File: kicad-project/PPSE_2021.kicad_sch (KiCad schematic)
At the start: 0 parts

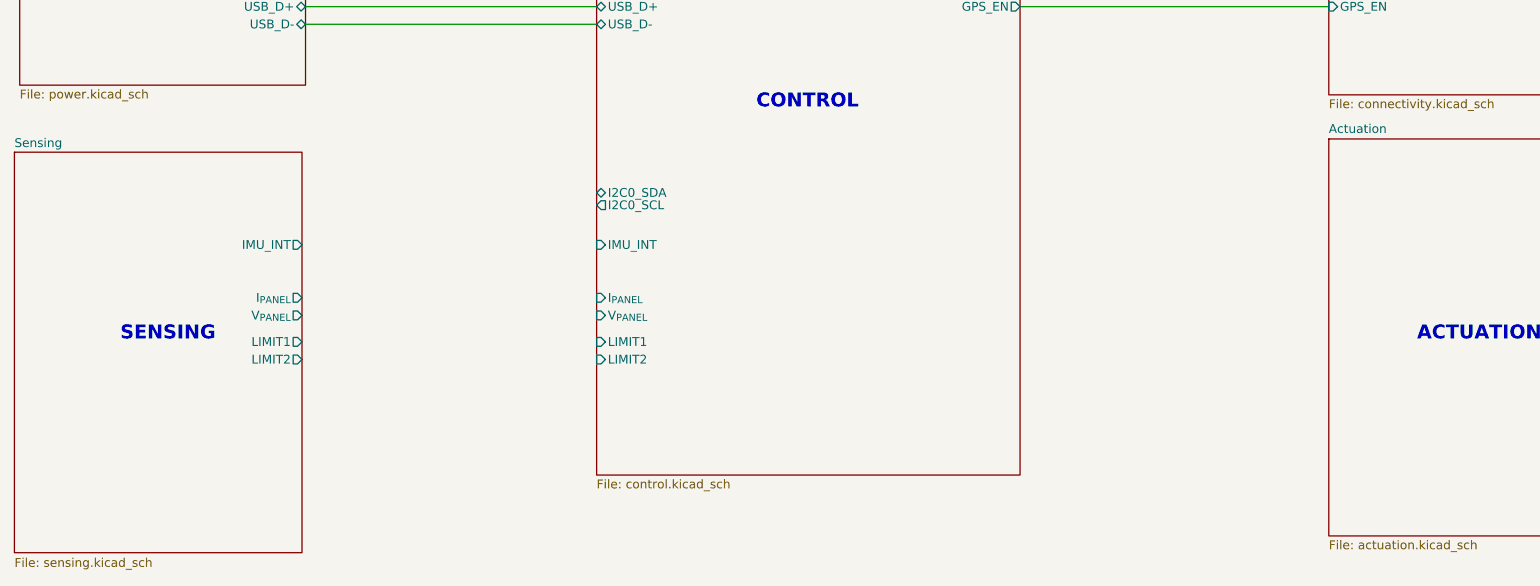
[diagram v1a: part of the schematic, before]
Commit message: hw: update root pin and usb connector
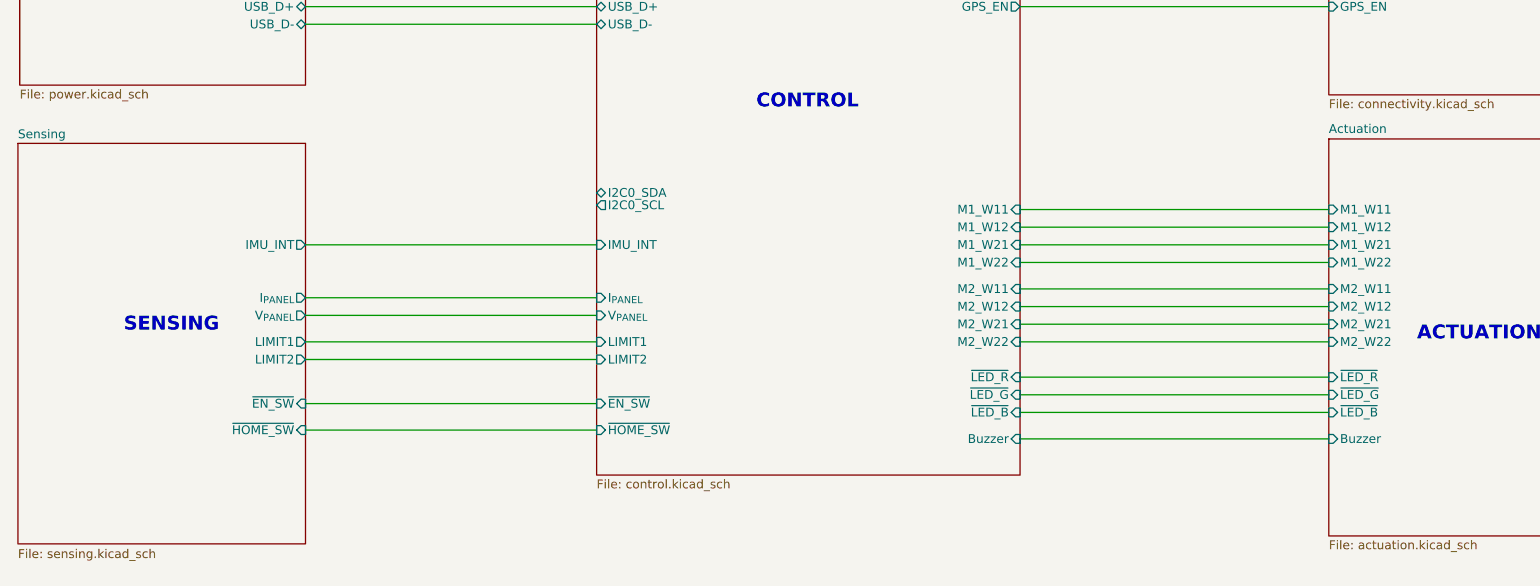
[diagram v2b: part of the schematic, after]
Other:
- sheet Actuation ports: added Buzzer, M1_W11, M1_W12, M1_W21, M1_W22, M2_W11, M2_W12, M2_W21, M2_W22, ~{LED_B}, ~{LED_G}, ~{LED_R}; removed none
- sheet Control ports: added Buzzer, M1_W11, M1_W12, M1_W21, M1_W22, M2_W11, M2_W12, M2_W21, M2_W22, ~{EN_SW}, ~{HOME_SW}, ~{LED_B}, ~{LED_G}, ~{LED_R}; removed none
- sheet Sensing ports: added ~{EN_SW}, ~{HOME_SW}; removed none
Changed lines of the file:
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@@
     (title "Main")
   )
+  (wire (pts (xy 71.12 111.76) (xy 113.03 111.76))
+    (stroke (width 0) (type default) (color 0 0 0 0))
+  )
+  (wire (pts (xy 173.99 116.84) (xy 218.44 116.84))
+    (stroke (width 0) (type default) (color 0 0 0 0))
+  )
+  (wire (pts (xy 173.99 92.71) (xy 218.44 92.71))
+    (stroke (width 0) (type default) (color 0 0 0 0))
+  )
+  (wire (pts (xy 71.12 120.65) (xy 113.03 120.65))
+    (stroke (width 0) (type default) (color 0 0 0 0))
+  )
   (wire (pts (xy 71.12 63.5) (xy 113.03 63.5))
     (stroke (width 0) (type default) (color 0 0 0 0))
   )
+  (wire (pts (xy 173.99 125.73) (xy 218.44 125.73))
+    (stroke (width 0) (type default) (color 0 0 0 0))
+  )
+  (wire (pts (xy 173.99 111.76) (xy 218.44 111.76))
+    (stroke (width 0) (type default) (color 0 0 0 0))
+  )
   (wire (pts (xy 173.99 60.96) (xy 218.44 60.96))
     (stroke (width 0) (type default) (color 0 0 0 0))
   )
+  (wire (pts (xy 173.99 104.14) (xy 218.44 104.14))
+    (stroke (width 0) (type default) (color 0 0 0 0))
+  )
+  (wire (pts (xy 173.99 106.68) (xy 218.44 106.68))
+    (stroke (width 0) (type default) (color 0 0 0 0))
+  )
   (wire (pts (xy 173.99 55.88) (xy 218.44 55.88))
     (stroke (width 0) (type default) (color 0 0 0 0))
   )
+  (wire (pts (xy 71.12 97.79) (xy 113.03 97.79))
+    (stroke (width 0) (type default) (color 0 0 0 0))
+  )
+  (wire (pts (xy 71.12 107.95) (xy 113.03 107.95))
+    (stroke (width 0) (type default) (color 0 0 0 0))
+  )
+  (wire (pts (xy 71.12 114.3) (xy 113.03 114.3))
+    (stroke (width 0) (type default) (color 0 0 0 0))
+  )
+  (wire (pts (xy 173.99 100.33) (xy 218.44 100.33))
+    (stroke (width 0) (type default) (color 0 0 0 0))
+  )
+  (wire (pts (xy 173.99 121.92) (xy 218.44 121.92))
+    (stroke (width 0) (type default) (color 0 0 0 0))
+  )
   (wire (pts (xy 218.44 63.5) (xy 173.99 63.5))
+    (stroke (width 0) (type default) (color 0 0 0 0))
+  )
+  (wire (pts (xy 173.99 95.25) (xy 218.44 95.25))
+    (stroke (width 0) (type default) (color 0 0 0 0))
+  )
+  (wire (pts (xy 71.12 124.46) (xy 113.03 124.46))
+    (stroke (width 0) (type default) (color 0 0 0 0))
+  )
+  (wire (pts (xy 173.99 97.79) (xy 218.44 97.79))
+    (stroke (width 0) (type default) (color 0 0 0 0))
+  )
+  (wire (pts (xy 71.12 105.41) (xy 113.03 105.41))
+    (stroke (width 0) (type default) (color 0 0 0 0))
+  )
+  (wire (pts (xy 173.99 109.22) (xy 218.44 109.22))
+    (stroke (width 0) (type default) (color 0 0 0 0))
+  )
+  (wire (pts (xy 173.99 119.38) (xy 218.44 119.38))
     (stroke (width 0) (type default) (color 0 0 0 0))
   )
@@
     (effects (font (size 2.0066 2.0066) (thickness 0.4013) bold) (justify left bottom))
   )
-  (text "SENSING" (at 44.45 111.76 0)
+  (text "SENSING" (at 44.958 110.49 0)
     (effects (font (size 2.0066 2.0066) (thickness 0.4013) bold) (justify left bottom))
   )
@@
       (effects (font (size 1.27 1.27)) (justify left))
     )
+    (pin "M2_W21" input (at 173.99 109.22 0)
+      (effects (font (size 1.27 1.27)) (justify right))
+    )
+    (pin "M1_W21" input (at 173.99 97.79 0)
+      (effects (font (size 1.27 1.27)) (justify right))
+    )
+    (pin "M1_W12" input (at 173.99 95.25 0)
+      (effects (font (size 1.27 1.27)) (justify right))
+    )
+    (pin "M1_W11" input (at 173.99 92.71 0)
+      (effects (font (size 1.27 1.27)) (justify right))
+    )
+    (pin "M2_W11" input (at 173.99 104.14 0)
+      (effects (font (size 1.27 1.27)) (justify right))
+    )
+    (pin "M2_W12" input (at 173.99 106.68 0)
+      (effects (font (size 1.27 1.27)) (justify right))
+    )
+    (pin "M1_W22" input (at 173.99 100.33 0)
+      (effects (font (size 1.27 1.27)) (justify right))
+    )
+    (pin "M2_W22" input (at 173.99 111.76 0)
+      (effects (font (size 1.27 1.27)) (justify right))
+    )
+    (pin "~{LED_R}" input (at 173.99 116.84 0)
+      (effects (font (size 1.27 1.27)) (justify right))
+    )
+    (pin "~{LED_B}" input (at 173.99 121.92 0)
+      (effects (font (size 1.27 1.27)) (justify right))
+    )
+    (pin "Buzzer" input (at 173.99 125.73 0)
+      (effects (font (size 1.27 1.27)) (justify right))
+    )
+    (pin "~{HOME_SW}" input (at 113.03 124.46 180)
+      (effects (font (size 1.27 1.27)) (justify left))
+    )
+    (pin "~{EN_SW}" input (at 113.03 120.65 180)
+      (effects (font (size 1.27 1.27)) (justify left))
+    )
+    (pin "~{LED_G}" input (at 173.99 119.38 0)
+      (effects (font (size 1.27 1.27)) (justify right))
+    )
   )
   (sheet (at 218.44 17.78) (size 41.91 58.42) (fields_autoplaced)
@@
       (effects (font (size 1.27 1.27)) (justify left top))
     )
-  )
-  (sheet (at 29.21 84.455) (size 41.402 57.658)
+    (pin "M1_W22" input (at 218.44 100.33 180)
+      (effects (font (size 1.27 1.27)) (justify left))
+    )
+    (pin "M1_W21" input (at 218.44 97.79 180)
+      (effects (font (size 1.27 1.27)) (justify left))
+    )
+    (pin "M2_W12" input (at 218.44 106.68 180)
+      (effects (font (size 1.27 1.27)) (justify left))
+    )
+    (pin "M2_W11" input (at 218.44 104.14 180)
+      (effects (font (size 1.27 1.27)) (justify left))
+    )
+    (pin "~{LED_B}" input (at 218.44 121.92 180)
+      (effects (font (size 1.27 1.27)) (justify left))
+    )
+    (pin "~{LED_G}" input (at 218.44 119.38 180)
+      (effects (font (size 1.27 1.27)) (justify left))
+    )
+    (pin "~{LED_R}" input (at 218.44 116.84 180)
+      (effects (font (size 1.27 1.27)) (justify left))
+    )
+    (pin "Buzzer" input (at 218.44 125.73 180)
+      (effects (font (size 1.27 1.27)) (justify left))
+    )
+    (pin "M1_W12" input (at 218.44 95.25 180)
+      (effects (font (size 1.27 1.27)) (justify left))
+    )
+    (pin "M1_W11" input (at 218.44 92.71 180)
+      (effects (font (size 1.27 1.27)) (justify left))
+    )
+    (pin "M2_W21" input (at 218.44 109.22 180)
+      (effects (font (size 1.27 1.27)) (justify left))
+    )
+    (pin "M2_W22" input (at 218.44 111.76 180)
+      (effects (font (size 1.27 1.27)) (justify left))
+    )
+  )
+  (sheet (at 29.718 83.185) (size 41.402 57.658)
     (stroke (width 0.1524) (type solid) (color 0 0 0 0))
     (fill (color 0 0 0 0.0000))
-    (property "Sheet name" "Sensing" (id 0) (at 29.21 83.8704 0)
+    (property "Sheet name" "Sensing" (id 0) (at 29.718 82.6004 0)
       (effects (font (size 1.27 1.27)) (justify left bottom))
     )
-    (property "Sheet file" "sensing.kicad_sch" (id 1) (at 29.21 142.8246 0)
+    (property "Sheet file" "sensing.kicad_sch" (id 1) (at 29.718 141.5546 0)
       (effects (font (size 1.27 1.27)) (justify left top))
     )
-    (pin "IMU_INT" output (at 70.612 97.79 0)
-      (effects (font (size 1.27 1.27)) (justify right))
-    )
-    (pin "I_{PANEL}" output (at 70.612 105.41 0)
-      (effects (font (size 1.27 1.27)) (justify right))
-    )
-    (pin "V_{PANEL}" output (at 70.612 107.95 0)
-      (effects (font (size 1.27 1.27)) (justify right))
-    )
-    (pin "LIMIT1" output (at 70.612 111.76 0)
-      (effects (font (size 1.27 1.27)) (justify right))
-    )
-    (pin "LIMIT2" output (at 70.612 114.3 0)
+    (pin "IMU_INT" output (at 71.12 97.79 0)
+      (effects (font (size 1.27 1.27)) (justify right))
+    )
+    (pin "I_{PANEL}" output (at 71.12 105.41 0)
+      (effects (font (size 1.27 1.27)) (justify right))
+    )
+    (pin "V_{PANEL}" output (at 71.12 107.95 0)
+      (effects (font (size 1.27 1.27)) (justify right))
+    )
+    (pin "LIMIT1" output (at 71.12 111.76 0)
+      (effects (font (size 1.27 1.27)) (justify right))
+    )
+    (pin "LIMIT2" output (at 71.12 114.3 0)
+      (effects (font (size 1.27 1.27)) (justify right))
+    )
+    (pin "~{EN_SW}" input (at 71.12 120.65 0)
+      (effects (font (size 1.27 1.27)) (justify right))
+    )
+    (pin "~{HOME_SW}" input (at 71.12 124.46 0)
       (effects (font (size 1.27 1.27)) (justify right))
     )
@@
     )
     (path "/00000000-0000-0000-0000-0000622d0e2d/9207196d-bb4d-46b0-8bb9-015d71d876e6"
-      (reference "J3") (unit 1) (value "USB_B_Micro") (footprint "Connector_USB:USB_Micro-B_Molex-105133-0001")
+      (reference "J3") (unit 1) (value "USB_B_Mini") (footprint "Connector_USB:USB_Micro-B_Molex-105133-0001")
     )
     (path "/00000000-0000-0000-0000-0000622d0e2d/00000000-0000-0000-0000-0000622e83ec"
@@
       (reference "J5") (unit 1) (value "Screw_Terminal_01x04") (footprint "TerminalBlock_TE-Connectivity:TerminalBlock_TE_282834-4_1x04_P2.54mm_Horizontal")
     )
-    (path "/e92ed148-d831-4ee6-93c4-e593d47b2e2f/e8cf4973-e2de-46f0-8ddf-999194cb2eee"
-      (reference "J6") (unit 1) (value "Conn_01x06") (footprint "Connector_PinHeader_2.54mm:PinHeader_1x06_P2.54mm_Vertical_SMD_Pin1Left")
-    )
     (path "/755090ec-fdfb-40aa-83ce-f20a94352e8e/d43b4e3f-930d-4cca-9e80-690431f9de68"
       (reference "J7") (unit 1) (value "Screw_Terminal_01x05") (footprint "TerminalBlock_TE-Connectivity:TerminalBlock_TE_282834-5_1x05_P2.54mm_Horizontal")
@@
       (reference "J9") (unit 1) (value "Conn_01x04") (footprint "Connector_PinHeader_2.54mm:PinHeader_1x04_P2.54mm_Vertical_SMD_Pin1Left")
     )
+    (path "/e92ed148-d831-4ee6-93c4-e593d47b2e2f/ec5ffa35-b0b2-4260-8371-175d881b43c9"
+      (reference "J?") (unit 1) (value "Conn_01x08") (footprint "")
+    )
     (path "/00000000-0000-0000-0000-00006222e27b/7d84260a-fa22-4d79-8c7a-214c2c72161d"

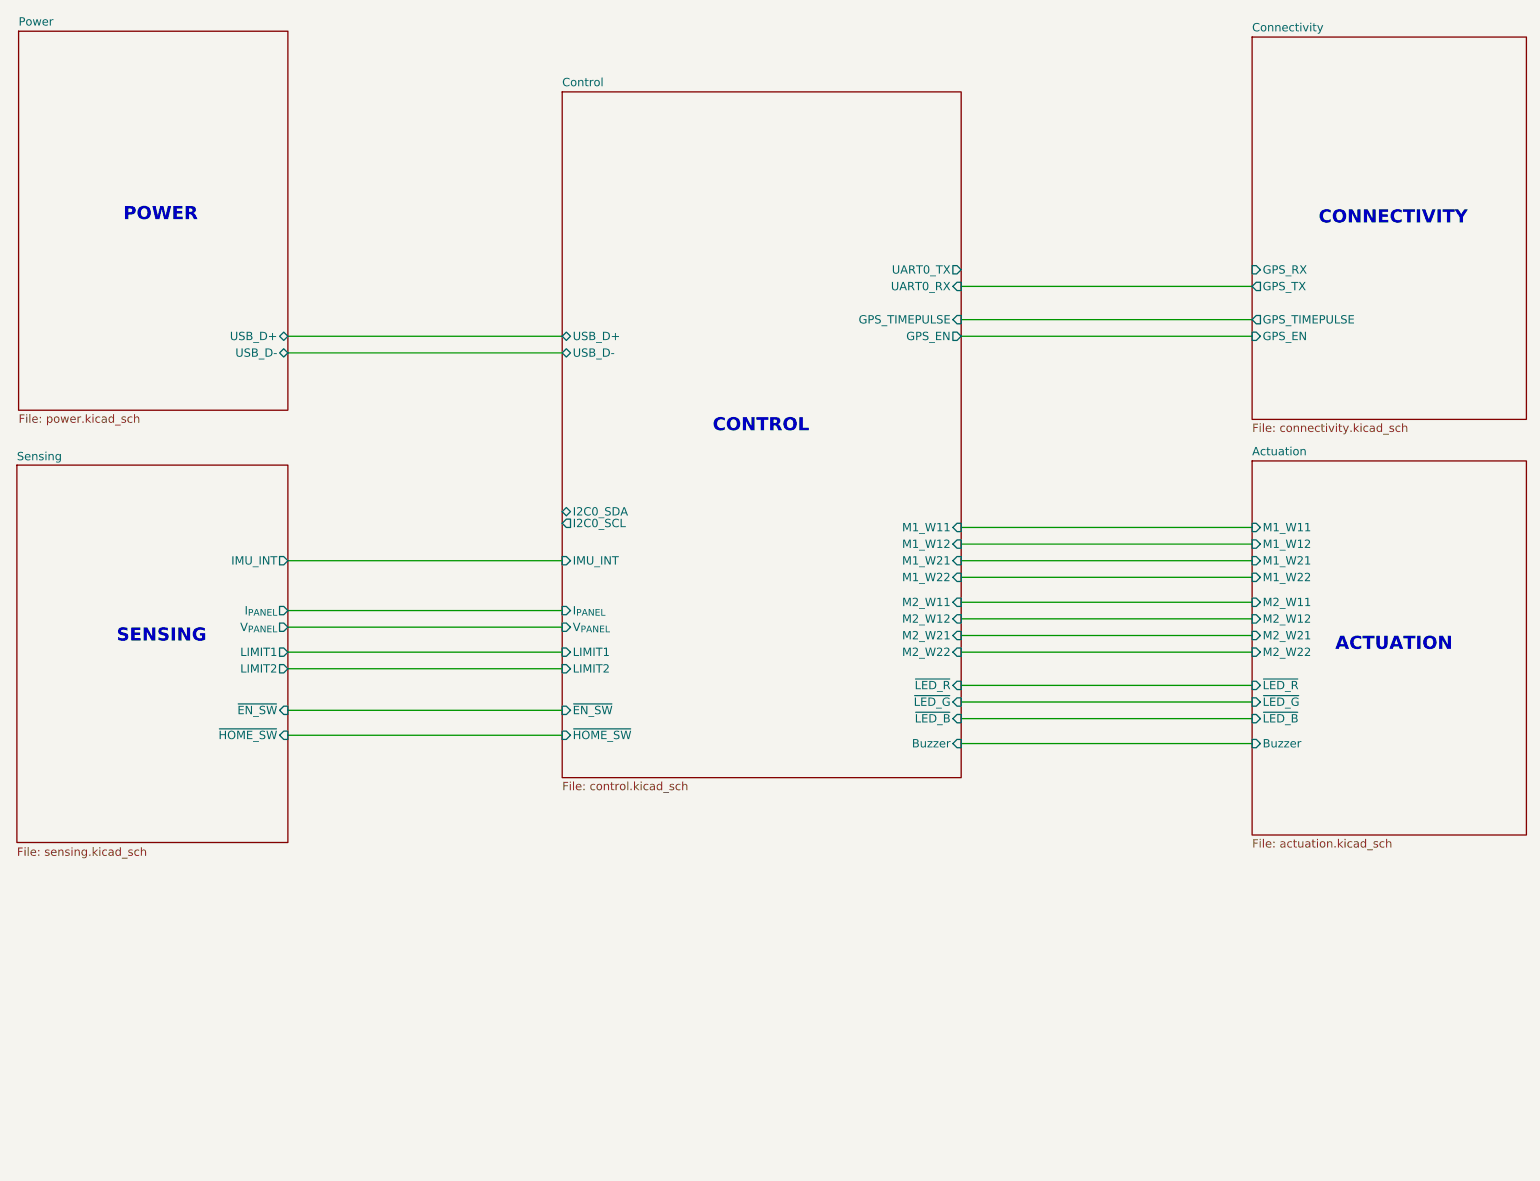
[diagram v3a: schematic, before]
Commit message: hw: part of last checks and footprint assignments
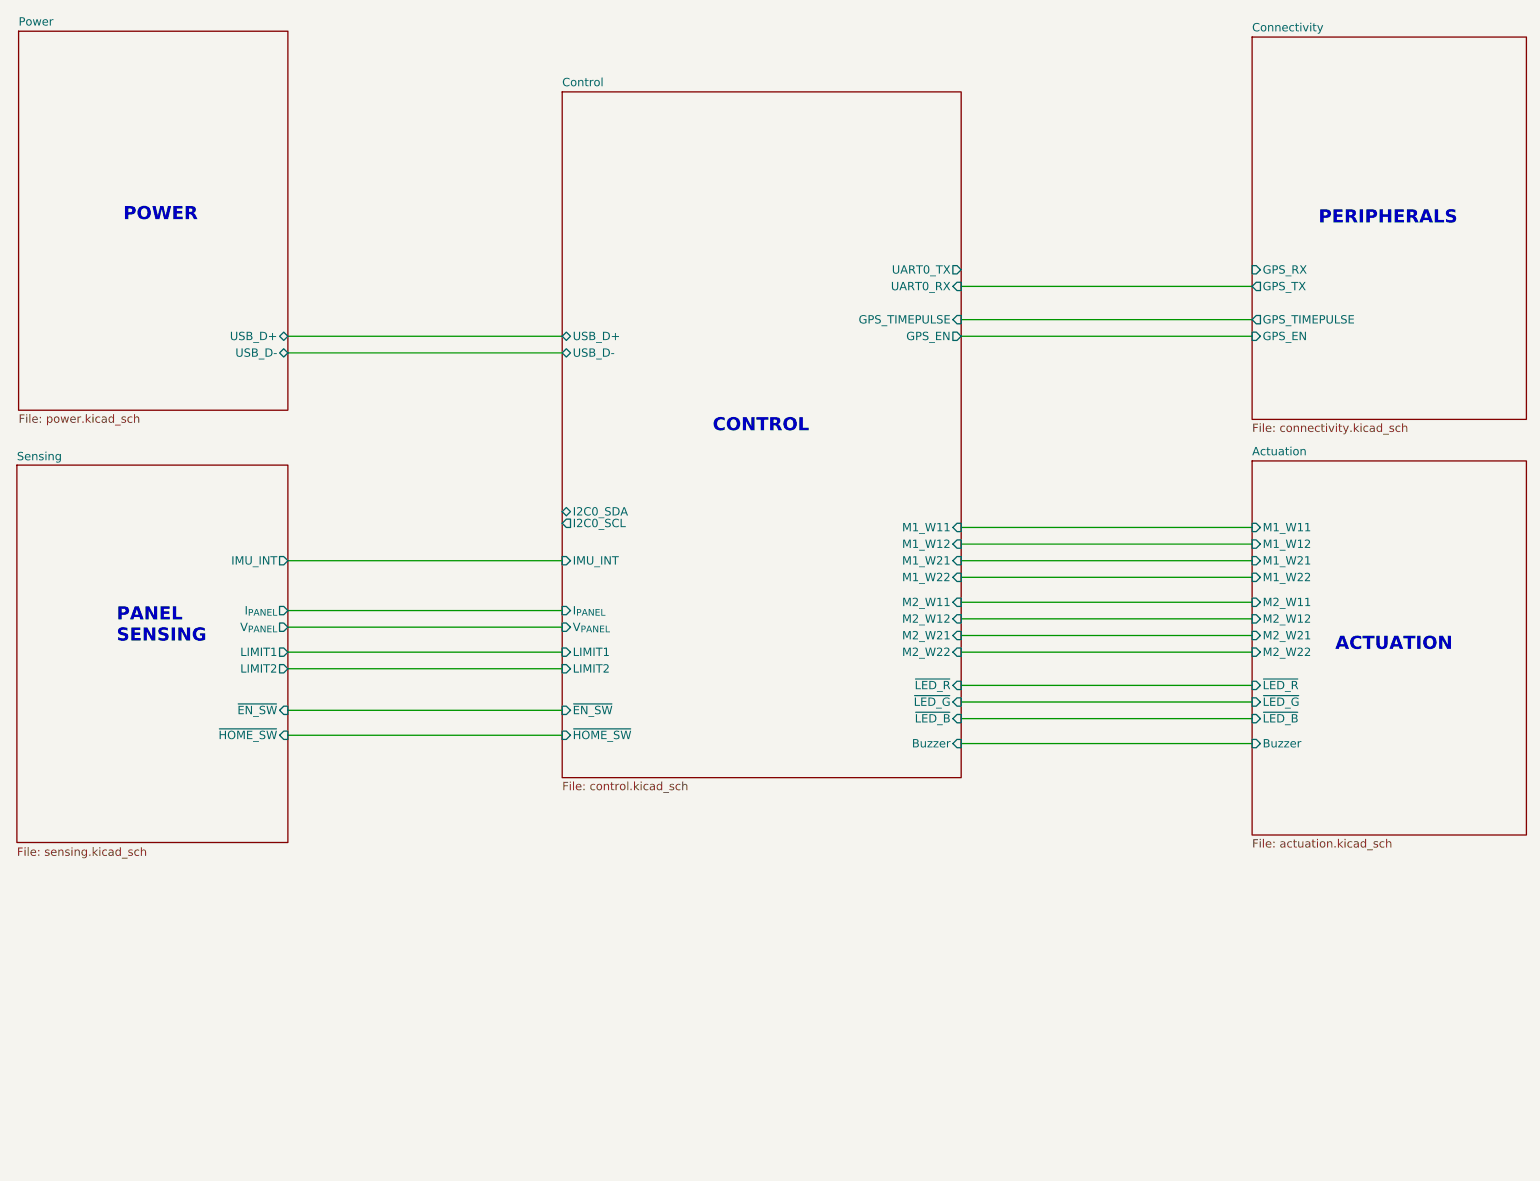
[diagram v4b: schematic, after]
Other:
- note added: "PANEL SENSING"
- note added: "PERIPHERALS"
- note removed: "CONNECTIVITY"
- note removed: "SENSING"

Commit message: commit anonimo di thimas
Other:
- sheet Control ports: added none; removed I2C0_SCL, I2C0_SDA

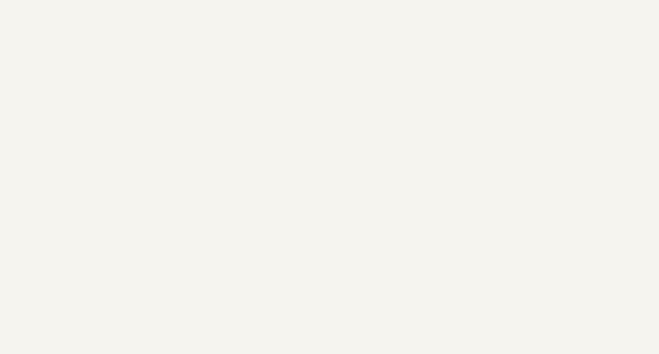
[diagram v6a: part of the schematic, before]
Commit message: hw: add mounting holes
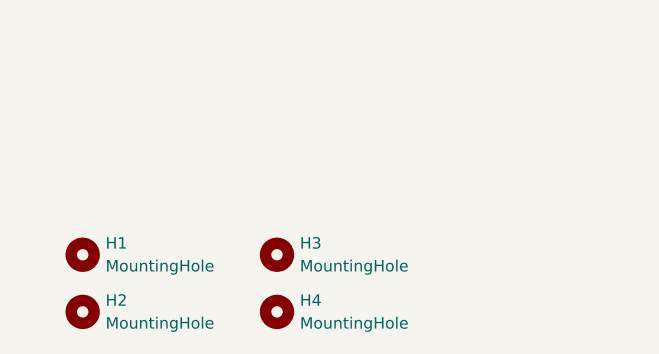
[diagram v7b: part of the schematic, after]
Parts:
- added H1, H2, H3, H4: MountingHole, MountingHole:MountingHole_3.2mm_M3, symbol Mechanical:MountingHole
